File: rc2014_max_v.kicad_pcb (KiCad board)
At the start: 4 copper layers, 101.6 x 50.8 mm, 127 parts, among them J1 M3 Mounting Hole, J2 Conn_01x40, J3 Conn_01x24, J4 USB_B_Micro, J5 AVR-JTAG-10, J6 Pro Bus, J7 PMOD1, J8 PMOD, J9 UPDI TTL, SW1 SW_Push, SW2 SW_Push, U1 TXB0108PWR, U10 ATtiny1614-SS, U11 5M1270ZT144C5N, U12 93LC46BT-I/OT, U13 IS61LV5128AL-10TLI, U14 Si5351A-B-GT, U15 TXB0108PWR, U16 TXB0108PWR, U18 MIC5356-SGYMME, U2 TXB0108PWR, U3 TXB0108PWR, U4 TXB0108PWR, U5 TXB0108PWR, U6 TXB0108PWR, U7 TXB0108PWR, U8 FT2232H, U9 TPD2EUSB30, X1 CB3LV-3I-100M0000, Y1 25MHZ 8PF

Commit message: started routing
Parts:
- removed C33: 100nF, Capacitor_SMD:C_0603_1608Metric_Pad1.05x0.95mm_HandSolder
- removed R12: 22R5, Resistor_SMD:R_0603_1608Metric_Pad1.05x0.95mm_HandSolder
- removed X1: CB3LV-3I-100M0000, Oscillator:Oscillator_SMD_SeikoEpson_SG8002CA-4Pin_7.0x5.0mm_HandSoldering
- J9: footprint Connector_PinHeader_2.54mm:PinHeader_1x03_P2.54mm_Horizontal -> Connector_PinHeader_2.54mm:PinHeader_1x03_P2.54mm_Vertical
- R17: moved to F.Cu
- moved C9 54.6 mm to (164.7, 104.0)
- moved J9 28.8 mm to (104.1, 109.7), turned to 90 degrees
- moved R17 23.9 mm to (106.6, 106.9)
- moved U12 18.6 mm to (150.9, 93.3)
- moved RN3 11.0 mm to (130.7, 85.3), turned to 270 degrees
- moved R16 8.68 mm to (122.7, 86.5)
- moved C31 7.03 mm to (117.9, 89.7)
- moved U14 5.74 mm to (115.4, 98.6)
- moved U10 5.57 mm to (107.2, 101.3)
- moved Y1 5.42 mm to (115.4, 102.7), turned to 0 degrees
- moved R11 5.17 mm to (146.1, 92.8), turned to 180 degrees
- moved R10 5.06 mm to (146.1, 94.5), turned to 180 degrees
- moved C3 4.19 mm to (127.9, 120.4), turned to 180 degrees
- moved C10 4.02 mm to (128.0, 114.2)
- moved R13 3.81 mm to (81.7, 118.5), turned to 90 degrees
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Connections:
- U11 pad 105: OE_C -> ~PAGE_F
- U11 pad 108: ~RESET_F -> OE_C
- U11 pad 109: ~PAGE_F -> (no net)
- U11 pad 110: CLK_F -> (no net)
- U11 pad 111: CLK2_F -> ~RESET_F
- U11 pad 18: CLK_7_3728_Mhz -> CLK2_F
- U11 pad 20: CLK_50Mhz -> CLK_F
- U11 pad 91: CLK_F -> CLK_7_3728_Mhz
- U14 pad 10: CLK_50Mhz -> CLK_100Mhz
- U4 pad 14: ~WR -> ~BUSRQ
- U4 pad 15: ~BUSRQ -> ~WR
- U4 pad 16: ~RD -> ~WAIT
- U4 pad 17: ~WAIT -> ~RD
- U4 pad 4: ~WAIT_F -> ~RD_F
- U4 pad 5: ~RD_F -> ~WAIT_F
- U4 pad 6: ~BUSRQ_F -> ~WR_F
- U4 pad 7: ~WR_F -> ~BUSRQ_F
- U5 pad 17: RXB -> TXA
- U5 pad 18: TXA -> RXB
- U5 pad 3: TXA_F -> RXB_F
- U5 pad 4: RXB_F -> TXA_F
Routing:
- net GND: track 0.00 -> 130.2 mm, vias 0 -> 5
- net ~PAGE_F: track 0.00 -> 18.0 mm
- net ~M1_F: track 0.00 -> 16.0 mm
- net ~RFSH~_F: track 0.00 -> 14.2 mm
- net 3V3: track 0.00 -> 12.4 mm, vias 0 -> 1
- net A15: track 0.00 -> 11.5 mm
- net A7: track 0.00 -> 11.2 mm
- net OE_C: track 0.00 -> 10.5 mm
- net A14: track 0.00 -> 9.51 mm
- net A6: track 0.00 -> 9.23 mm
- net D6: track 0.00 -> 8.48 mm
- net D7: track 0.00 -> 8.47 mm
- net ~BUSACK_F: track 0.00 -> 8.38 mm
- net ~M1: track 0.00 -> 7.90 mm
- net A13: track 0.00 -> 7.90 mm
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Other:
- copper layers 4 -> 2
- board text added: "UDPI"
- board text added: "VCC Select"
- board text removed: "100 Mhz"
- board text removed: "12Mhz"

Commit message: mirror flipped the chips
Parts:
- removed D6, D7, D8, D9: Red, LED_SMD:LED_0603_1608Metric_Pad1.05x0.95mm_HandSolder
- moved SW2 94.2 mm to (170.0, 80.8), turned to 0 degrees
- moved R14 93.2 mm to (173.2, 83.6), turned to 180 degrees
- moved C37 90.6 mm to (169.8, 83.6), turned to 180 degrees
- moved U9 89.9 mm to (81.7, 101.3), turned to 0 degrees
- moved J4 88.3 mm to (85.3, 87.2), turned to 45 degrees
- moved JP2 87.5 mm to (79.5, 106.0), turned to 180 degrees
- moved C23 78.1 mm to (91.0, 89.0), turned to 270 degrees
- moved R7 77.7 mm to (89.4, 89.0), turned to 270 degrees
- moved RN2 75.5 mm to (85.7, 110.0)
- moved RN6 74.7 mm to (71.4, 79.9)
- moved JP1 65.5 mm to (157.9, 85.1)
- moved C30 61.3 mm to (91.0, 106.2)
- moved C29 61.0 mm to (84.0, 100.2)
- moved U8 59.9 mm to (91.0, 100.4), turned to 0 degrees
- moved C28 59.9 mm to (96.7, 100.3)
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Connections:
- C38 pad 1: GND -> +3V3
- C39 pad 1: GND -> +3V3
- C40 pad 1: GND -> +3V3
- C41 pad 1: GND -> +3V3
- J7 pad 12: GND -> +3V3
- J7 pad 6: GND -> +3V3
- J8 pad 12: GND -> +3V3
- J8 pad 6: GND -> +3V3
- RN3 pad 2: JTAG_TMS -> JTAG_TDO
- RN3 pad 3: JTAG_TDO -> JTAG_TMS
- RN5 pad 5: GND -> 3V3
- RN5 pad 6: GND -> 3V3
- RN5 pad 7: GND -> 3V3
- RN5 pad 8: GND -> 3V3
- U13 pad 11: GND -> 3V3
- U13 pad 33: GND -> 3V3
- U16 pad 12: GPIO_16 -> GPIO_13
- U16 pad 13: GPIO_15 -> GPIO_14
- U16 pad 14: GPIO_14 -> GPIO_15
- U16 pad 15: GPIO_13 -> GPIO_16
- U16 pad 6: GPIO_13_F -> GPIO_16_F
- U16 pad 7: GPIO_14_F -> GPIO_15_F
- U16 pad 8: GPIO_15_F -> GPIO_14_F
- U16 pad 9: GPIO_16_F -> GPIO_13_F
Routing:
- net GND: track 130.2 -> 48.5 mm, vias 5 -> 15
- net ~PAGE_F: track 18.0 -> 0.00 mm
- net 5V: track 6.63 -> 22.3 mm, vias 2 -> 3
- net ~M1_F: track 16.0 -> 0.66 mm
- net ~RFSH~_F: track 14.2 -> 0.00 mm
- net A15: track 11.5 -> 0.00 mm
- net A7: track 11.2 -> 0.00 mm
- net A14: track 9.51 -> 0.00 mm
- net A6: track 9.23 -> 0.00 mm
- net OE_C: track 10.5 -> 2.32 mm
- net A13: track 7.90 -> 0.00 mm
- net A8: track 7.84 -> 0.00 mm
- net A0: track 7.78 -> 0.00 mm
- net A5: track 7.75 -> 0.00 mm
- net ~BUSACK_F: track 8.38 -> 0.71 mm
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- added copper zone on In1.Cu, net 3V3
- added copper zone on In1.Cu, net 5V
- added copper zone on In2.Cu, net GND
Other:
- copper layers 2 -> 4
- board text added: "5V Select"
- board text added: "LED[0..3]"
- board text removed: "LED[1..8]"
- board text removed: "RC2014 MAX V Development Board v0.1 by Hyiger Designs"
- board text removed: "VCC Select"

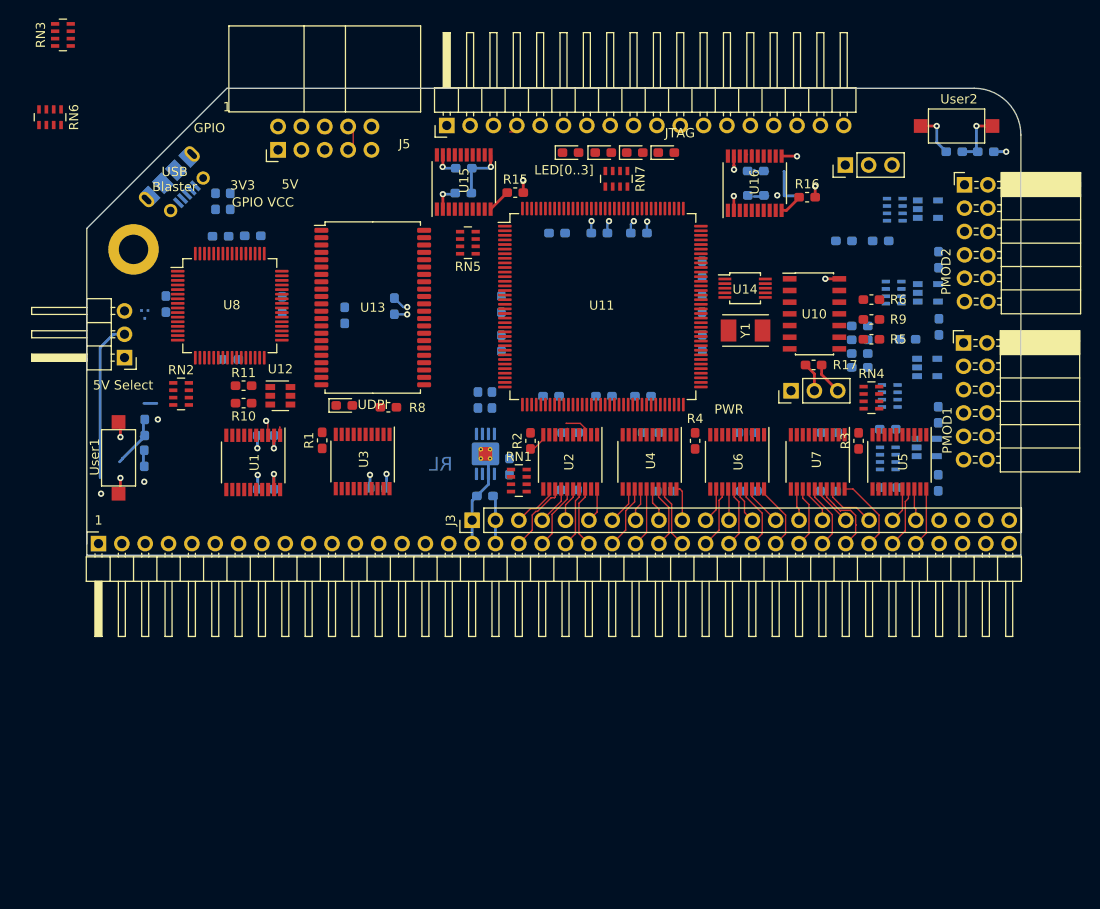
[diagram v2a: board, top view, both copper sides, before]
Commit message: moved things around to improve routing, fixed power plane
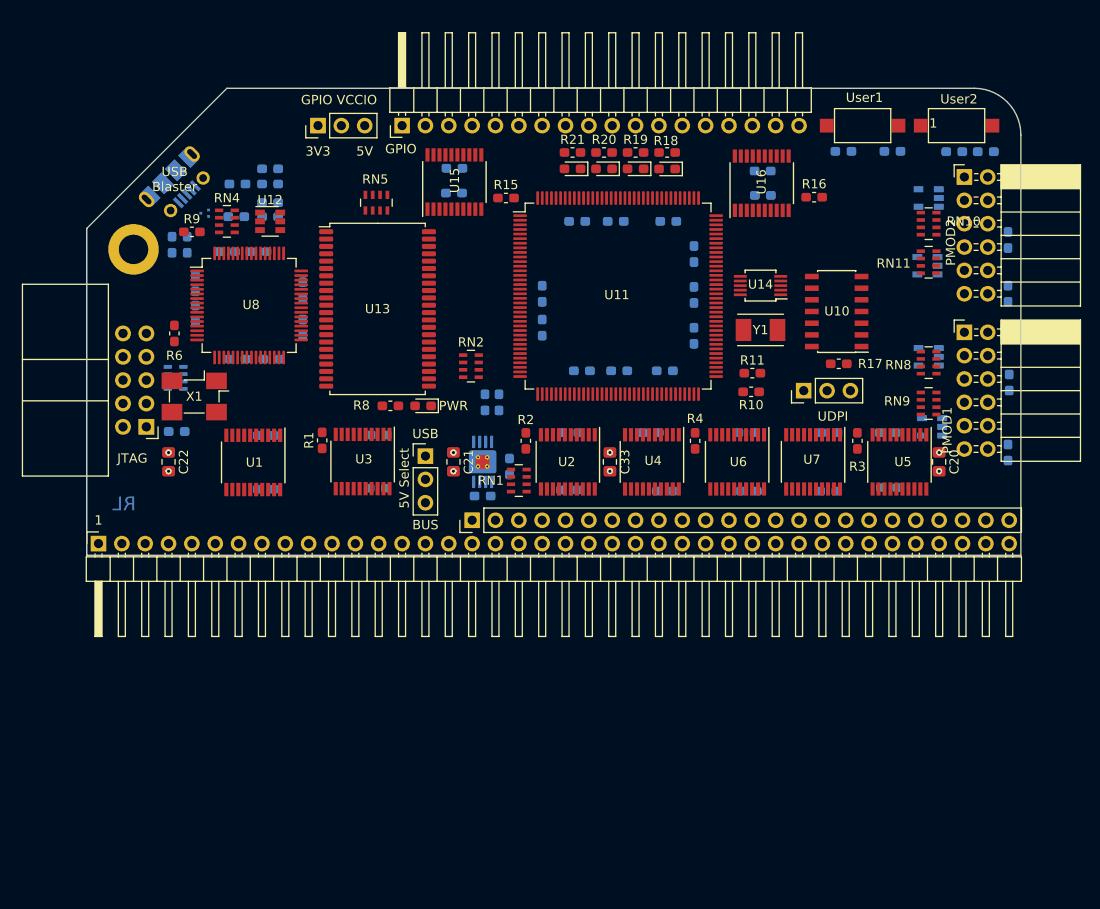
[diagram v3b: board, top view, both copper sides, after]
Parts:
- removed D2, D3, D4, D5: Red, LED_SMD:LED_0603_1608Metric_Pad1.05x0.95mm_HandSolder
- removed RN6, RN7: 270R, Resistor_SMD:R_Array_Concave_4x0603
- added C20: 100nF, Capacitor_SMD:C_0805_2012Metric_Pad1.15x1.40mm_HandSolder, F.Cu at (168.1, 117.3)
- added C21: 100nF, Capacitor_SMD:C_0805_2012Metric_Pad1.15x1.40mm_HandSolder, F.Cu at (115.3, 117.3)
- added C22: 100nF, Capacitor_SMD:C_0805_2012Metric_Pad1.15x1.40mm_HandSolder, F.Cu at (84.3, 117.3)
- added C33: 100nF, Capacitor_SMD:C_0805_2012Metric_Pad1.15x1.40mm_HandSolder, F.Cu at (132.3, 117.3)
- added LED1: Red, LED_SMD:LED_0603_1608Metric_Pad1.05x0.95mm_HandSolder, F.Cu at (128.3, 85.5)
- added LED2: Red, LED_SMD:LED_0603_1608Metric_Pad1.05x0.95mm_HandSolder, F.Cu at (131.7, 85.5)
- added LED3: Red, LED_SMD:LED_0603_1608Metric_Pad1.05x0.95mm_HandSolder, F.Cu at (135.1, 85.5)
- added LED4: Red, LED_SMD:LED_0603_1608Metric_Pad1.05x0.95mm_HandSolder, F.Cu at (138.6, 85.5)
- added R12: 1K, Resistor_SMD:R_0603_1608Metric_Pad1.05x0.95mm_HandSolder, B.Cu at (85.2, 114.0)
- added R18: 270R, Resistor_SMD:R_0603_1608Metric_Pad1.05x0.95mm_HandSolder, F.Cu at (138.6, 83.7)
- added R19: 270R, Resistor_SMD:R_0603_1608Metric_Pad1.05x0.95mm_HandSolder, F.Cu at (135.1, 83.7)
- added R20: 270R, Resistor_SMD:R_0603_1608Metric_Pad1.05x0.95mm_HandSolder, F.Cu at (131.7, 83.7)
- added R21: 270R, Resistor_SMD:R_0603_1608Metric_Pad1.05x0.95mm_HandSolder, F.Cu at (128.3, 83.7)
- added X1: KC5032K12.0000C10E00, Oscillator:Oscillator_SMD_Fordahl_DFAS15-4Pin_5.0x3.2mm_HandSoldering, F.Cu at (87.1, 110.2)
- J8: value PMOD -> PMOD2
- JP2: footprint Connector_PinHeader_2.54mm:PinHeader_1x03_P2.54mm_Horizontal -> Connector_PinHeader_2.54mm:PinHeader_1x03_P2.54mm_Vertical
- R5, RN3: moved to B.Cu
- RN10, RN11, RN8, RN9: moved to F.Cu
- moved SW1 88.6 mm to (159.8, 80.8), turned to 180 degrees
- moved C36 88.0 mm to (163.1, 83.6), turned to 0 degrees
- moved R13 81.7 mm to (157.7, 83.6), turned to 0 degrees
- moved R6 75.9 mm to (85.0, 103.4), turned to 90 degrees
- moved R9 74.5 mm to (86.9, 92.3)
- moved R5 73.8 mm to (87.2, 97.9), turned to 270 degrees
- moved RN4 72.7 mm to (90.7, 91.2), turned to 180 degrees
- moved L1 70.1 mm to (91.7, 90.7)
- moved C19 67.7 mm to (95.4, 85.5)
- moved C18 66.7 mm to (95.4, 87.1)
- moved L2 66.3 mm to (91.8, 87.1)
- moved C17 65.8 mm to (95.4, 89.2)
- moved C16 65.2 mm to (95.4, 90.7)
- moved C9 58.5 mm to (107.2, 114.4)
- moved JP1 57.5 mm to (100.6, 80.8)
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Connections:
- C38 pad 1: +3V3 -> 3V3
- C39 pad 1: +3V3 -> 3V3
- C40 pad 1: +3V3 -> 3V3
- C41 pad 1: +3V3 -> 3V3
- J7 pad 12: +3V3 -> 3V3
- J7 pad 6: +3V3 -> 3V3
- J8 pad 12: +3V3 -> 3V3
- J8 pad 6: +3V3 -> 3V3
- RN3 pad 1: JTAG_TCK -> JTAG_TDO
- RN3 pad 2: JTAG_TDO -> JTAG_TMS
- RN3 pad 3: JTAG_TMS -> JTAG_TDI
- RN3 pad 4: JTAG_TDI -> (no net)
- RN3 pad 5: 3V3 -> (no net)
- RN3 pad 8: GND -> 3V3
- U11 pad 1: TXB_F -> SCL
- U11 pad 101: A2_F -> PMOD2_8
- U11 pad 102: A1_F -> PMOD2_1
- U11 pad 103: A0_F -> PMOD2_2
- U11 pad 104: OE_A -> PMOD2_3
- U11 pad 105: ~PAGE_F -> PMOD2_4
- U11 pad 106: ~M1_F -> (no net)
- U11 pad 107: ~RFSH~_F -> SW_USER2
- U11 pad 108: OE_C -> SW_USER1
- U11 pad 109: (no net) -> GPIO_16_F
- U11 pad 110: (no net) -> GPIO_15_F
- U11 pad 111: ~RESET_F -> GPIO_14_F
- U11 pad 112: ~INT_F -> GPIO_13_F
- U11 pad 113: ~BUSACK_F -> GPIO_12_F
- U11 pad 114: ~MREQ_F -> GPIO_11_F
- U11 pad 117: ~HALT_F -> GPIO_10_F
- U11 pad 118: ~WR_F -> GPIO_9_F
- U11 pad 119: ~BUSRQ_F -> (no net)
- U11 pad 12: PMOD2_6 -> A12_F
- U11 pad 120: ~RD_F -> (no net)
- U11 pad 121: ~WAIT_F -> (no net)
- U11 pad 122: ~IORQ_F -> (no net)
- U11 pad 123: ~NMI_F -> LED4
- U11 pad 124: OE_D -> LED3
- U11 pad 125: D8_F -> LED2
- U11 pad 127: D0_F -> LED1
- U11 pad 129: D9_F -> (no net)
- U11 pad 13: PMOD2_7 -> A11_F
- U11 pad 130: D1_F -> (no net)
- U11 pad 131: D10_F -> (no net)
- U11 pad 132: D2_F -> (no net)
- U11 pad 133: D11_F -> (no net)
- U11 pad 134: D3_F -> GPIO_8_F
- U11 pad 137: D12_F -> GPIO_7_F
- U11 pad 138: D4_F -> GPIO_6_F
- U11 pad 139: D13_F -> GPIO_5_F
- U11 pad 14: PMOD2_8 -> A10_F
- U11 pad 140: D5_F -> GPIO_4_F
- U11 pad 141: D14_F -> GPIO_3_F
- U11 pad 142: D6_F -> GPIO_2_F
- U11 pad 143: D15_F -> GPIO_1_F
- U11 pad 144: D7_F -> OE_G
- U11 pad 15: PMOD2_1 -> A9_F
- U11 pad 16: PMOD2_2 -> A8_F
- U11 pad 18: CLK2_F -> CLK_1Mhz
- U11 pad 2: RXB_F -> SDA
- U11 pad 21: PMOD2_3 -> A7_F
- U11 pad 22: PMOD2_4 -> A6_F
- U11 pad 23: PMOD1_8 -> A5_F
- U11 pad 24: PMOD1_7 -> A4_F
- U11 pad 27: PMOD1_6 -> A3_F
- U11 pad 28: PMOD1_5 -> A2_F
- U11 pad 29: PMOD1_1 -> A1_F
- U11 pad 3: TXA_F -> ~OE~_RAM
- U11 pad 30: PMOD1_2 -> A0_F
- U11 pad 31: PMOD1_3 -> OE_A
- U11 pad 32: PMOD1_4 -> (no net)
- U11 pad 37: SCL -> OE_C
- U11 pad 38: SDA -> ~RFSH~_F
- U11 pad 39: (no net) -> ~M1_F
- U11 pad 4: RXA_F -> ~CE~_RAM
- U11 pad 40: (no net) -> ~PAGE_F
- U11 pad 41: LED8 -> ~RESET_F
- U11 pad 42: LED7 -> ~INT_F
- U11 pad 43: LED6 -> ~BUSACK_F
- U11 pad 44: LED5 -> ~HALT_F
- U11 pad 45: LED4 -> ~MREQ_F
- U11 pad 48: LED3 -> ~BUSRQ_F
- U11 pad 49: LED2 -> ~WR_F
- U11 pad 5: OE_S -> A15_F
- U11 pad 50: LED1 -> ~WAIT_F
- U11 pad 51: (no net) -> ~RD_F
- U11 pad 52: OE_G -> ~IORQ_F
- U11 pad 53: GPIO_16_F -> ~NMI_F
- U11 pad 55: GPIO_15_F -> OE_D
- U11 pad 57: GPIO_14_F -> D8_F
- U11 pad 58: GPIO_13_F -> D0_F
- U11 pad 59: GPIO_12_F -> D9_F
- U11 pad 6: (no net) -> ~WE~_RAM
- U11 pad 60: GPIO_11_F -> D1_F
- U11 pad 61: GPIO_10_F -> D10_F
- U11 pad 62: GPIO_9_F -> D2_F
- U11 pad 63: GPIO_8_F -> D11_F
- U11 pad 66: GPIO_7_F -> D3_F
- U11 pad 67: GPIO_6_F -> D12_F
- U11 pad 68: GPIO_5_F -> D4_F
- U11 pad 69: GPIO_4_F -> D13_F
- U11 pad 7: (no net) -> A14_F
- U11 pad 70: GPIO_3_F -> D5_F
- U11 pad 71: GPIO_2_F -> D14_F
- U11 pad 72: GPIO_1_F -> (no net)
- U11 pad 73: SW_USER2 -> D6_F
- U11 pad 74: SW_USER1 -> D15_F
- U11 pad 75: (no net) -> D7_F
- U11 pad 76: ~OE~_RAM -> TXB_F
- U11 pad 77: ~WE~_RAM -> RXB_F
- U11 pad 79: ~CE~_RAM -> TXA_F
- U11 pad 8: PMOD2_5 -> A13_F
- U11 pad 80: A15_F -> RXA_F
- U11 pad 81: A13_F -> OE_S
- U11 pad 84: A14_F -> PMOD1_8
- U11 pad 85: A12_F -> PMOD1_7
- U11 pad 86: A11_F -> PMOD1_6
- U11 pad 87: A10_F -> PMOD1_5
- U11 pad 88: A9_F -> PMOD1_1
- U11 pad 93: A8_F -> PMOD1_2
- U11 pad 94: A7_F -> PMOD1_3
- U11 pad 95: A6_F -> PMOD1_4
- U11 pad 96: A5_F -> PMOD2_5
- U11 pad 97: A4_F -> PMOD2_6
- U11 pad 98: A3_F -> PMOD2_7
- U14 pad 6: CLK_7_3728_Mhz -> CLK_1Mhz
- U14 pad 9: CLK_12Mhz -> CLK_7_3728_Mhz
- U16 pad 12: GPIO_13 -> GPIO_16
- U16 pad 13: GPIO_14 -> GPIO_15
- U16 pad 14: GPIO_15 -> GPIO_14
- U16 pad 15: GPIO_16 -> GPIO_13
- U16 pad 6: GPIO_16_F -> GPIO_13_F
- U16 pad 7: GPIO_15_F -> GPIO_14_F
- U16 pad 8: GPIO_14_F -> GPIO_15_F
- U16 pad 9: GPIO_13_F -> GPIO_16_F
- U2 pad 5: CLK2_F -> (no net)
- U5 pad 12: (no net) -> GND
- U5 pad 13: (no net) -> GND
- U5 pad 14: (no net) -> GND
- U5 pad 15: (no net) -> GND
- U5 pad 6: (no net) -> GND
- U5 pad 7: (no net) -> GND
- U5 pad 8: (no net) -> GND
- U5 pad 9: (no net) -> GND
- U8 pad 2: CLK_12Mhz -> Net-(U8-Pad2)
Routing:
- net GND: track 48.5 -> 0.00 mm, vias 15 -> 0
- net 5V: track 22.3 -> 0.00 mm, vias 3 -> 4
- net 3V3: track 13.9 -> 0.00 mm, vias 7 -> 4
- net D6: track 8.48 -> 0.00 mm
- net D7: track 8.47 -> 0.00 mm
- net ~M1: track 7.90 -> 0.00 mm
- net D3: track 7.36 -> 0.00 mm
- net SW_USER1: track 7.30 -> 0.00 mm, vias 1 -> 0
- net D5: track 7.18 -> 0.00 mm
- net D2: track 7.11 -> 0.00 mm
- net ~RESET: track 7.07 -> 0.00 mm
- net ~MREQ: track 6.95 -> 0.00 mm
- net ~RD: track 6.85 -> 0.00 mm
- net ~IORQ: track 6.74 -> 0.00 mm
- net D0: track 6.69 -> 0.00 mm
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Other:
- board text added: "BUS"
- board text added: "GPIO VCCIO"
- board text added: "USB"
- board text removed: "GPIO VCC"
- board text removed: "LED[0..3]"
